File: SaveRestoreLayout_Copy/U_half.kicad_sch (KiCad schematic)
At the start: 2 parts

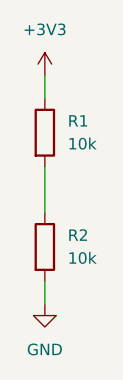
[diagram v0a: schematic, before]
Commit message: annotate the copy of SaveRestoreLayout_Copy/U_half.kicad_sch
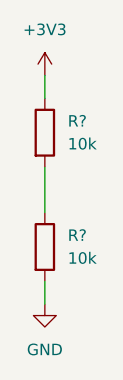
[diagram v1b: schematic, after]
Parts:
- renumbered R2 to R?, R1 to R?
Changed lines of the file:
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@@
   (symbol (lib_id "Device:R") (at 123.19 88.9 0) (unit 1)
     (in_bom yes) (on_board yes) (dnp no) (fields_autoplaced)
-    (property "Reference" "R2" (at 125.73 87.63 0)
+    (property "Reference" "R?" (at 125.73 87.63 0)
       (effects (font (size 1.27 1.27)) (justify left))
     )
@@
       (project "SaveRestoreLayout_Original"
         (path "/77dfa459-80c3-47cd-804e-1711acb5c83d/a587b1de-fcac-40bf-8a11-56b95432cd59"
-          (reference "R2") (unit 1)
+          (reference "R?") (unit 1)
+        )
+      )
+      (project "SaveRestoreLayout_Copy"
+        (path "/f7049a7e-2ee3-423f-8203-c90463fac327/9e96eef9-761d-4371-b289-d9fc0db18200"
+          (reference "R3") (unit 1)
         )
       )
@@
   (symbol (lib_id "power:+3V3") (at 123.19 69.85 0) (unit 1)
     (in_bom yes) (on_board yes) (dnp no) (fields_autoplaced)
-    (property "Reference" "#PWR03" (at 123.19 73.66 0)
+    (property "Reference" "#PWR?" (at 123.19 73.66 0)
       (effects (font (size 1.27 1.27)) hide)
     )
@@
       (project "SaveRestoreLayout_Original"
         (path "/77dfa459-80c3-47cd-804e-1711acb5c83d/a587b1de-fcac-40bf-8a11-56b95432cd59"
+          (reference "#PWR?") (unit 1)
+        )
+      )
+      (project "SaveRestoreLayout_Copy"
+        (path "/f7049a7e-2ee3-423f-8203-c90463fac327/9e96eef9-761d-4371-b289-d9fc0db18200"
           (reference "#PWR03") (unit 1)
         )
@@
   (symbol (lib_id "power:GND") (at 123.19 95.25 0) (unit 1)
     (in_bom yes) (on_board yes) (dnp no) (fields_autoplaced)
-    (property "Reference" "#PWR04" (at 123.19 101.6 0)
+    (property "Reference" "#PWR?" (at 123.19 101.6 0)
       (effects (font (size 1.27 1.27)) hide)
     )
@@
       (project "SaveRestoreLayout_Original"
         (path "/77dfa459-80c3-47cd-804e-1711acb5c83d/a587b1de-fcac-40bf-8a11-56b95432cd59"
+          (reference "#PWR?") (unit 1)
+        )
+      )
+      (project "SaveRestoreLayout_Copy"
+        (path "/f7049a7e-2ee3-423f-8203-c90463fac327/9e96eef9-761d-4371-b289-d9fc0db18200"
           (reference "#PWR04") (unit 1)
         )
@@
   (symbol (lib_id "Device:R") (at 123.19 76.2 0) (unit 1)
     (in_bom yes) (on_board yes) (dnp no) (fields_autoplaced)
-    (property "Reference" "R1" (at 125.73 74.93 0)
+    (property "Reference" "R?" (at 125.73 74.93 0)
       (effects (font (size 1.27 1.27)) (justify left))
     )
@@
       (project "SaveRestoreLayout_Original"
         (path "/77dfa459-80c3-47cd-804e-1711acb5c83d/a587b1de-fcac-40bf-8a11-56b95432cd59"
-          (reference "R1") (unit 1)
+          (reference "R?") (unit 1)
         )
       )
+      (project "SaveRestoreLayout_Copy"
+        (path "/f7049a7e-2ee3-423f-8203-c90463fac327/9e96eef9-761d-4371-b289-d9fc0db18200"
+          (reference "R2") (unit 1)
+        )
+      )

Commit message: restore the layour from original
bug: the bottom layout is not restored and no via is placed
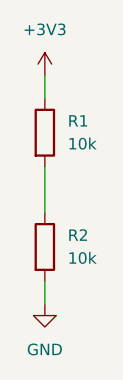
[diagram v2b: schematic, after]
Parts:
- gave numbers to parts that had none: 2
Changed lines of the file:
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@@
   (symbol (lib_id "Device:R") (at 123.19 88.9 0) (unit 1)
     (in_bom yes) (on_board yes) (dnp no) (fields_autoplaced)
-    (property "Reference" "R?" (at 125.73 87.63 0)
+    (property "Reference" "R2" (at 125.73 87.63 0)
       (effects (font (size 1.27 1.27)) (justify left))
     )
@@
       (project "SaveRestoreLayout_Original"
         (path "/77dfa459-80c3-47cd-804e-1711acb5c83d/a587b1de-fcac-40bf-8a11-56b95432cd59"
-          (reference "R?") (unit 1)
+          (reference "R2") (unit 1)
         )
       )
       (project "SaveRestoreLayout_Copy"
         (path "/f7049a7e-2ee3-423f-8203-c90463fac327/9e96eef9-761d-4371-b289-d9fc0db18200"
-          (reference "R3") (unit 1)
+          (reference "R2") (unit 1)
         )
       )
@@
   (symbol (lib_id "power:+3V3") (at 123.19 69.85 0) (unit 1)
     (in_bom yes) (on_board yes) (dnp no) (fields_autoplaced)
-    (property "Reference" "#PWR?" (at 123.19 73.66 0)
+    (property "Reference" "#PWR03" (at 123.19 73.66 0)
       (effects (font (size 1.27 1.27)) hide)
     )
@@
       (project "SaveRestoreLayout_Original"
         (path "/77dfa459-80c3-47cd-804e-1711acb5c83d/a587b1de-fcac-40bf-8a11-56b95432cd59"
-          (reference "#PWR?") (unit 1)
+          (reference "#PWR03") (unit 1)
         )
       )
@@
   (symbol (lib_id "power:GND") (at 123.19 95.25 0) (unit 1)
     (in_bom yes) (on_board yes) (dnp no) (fields_autoplaced)
-    (property "Reference" "#PWR?" (at 123.19 101.6 0)
+    (property "Reference" "#PWR04" (at 123.19 101.6 0)
       (effects (font (size 1.27 1.27)) hide)
     )
@@
       (project "SaveRestoreLayout_Original"
         (path "/77dfa459-80c3-47cd-804e-1711acb5c83d/a587b1de-fcac-40bf-8a11-56b95432cd59"
-          (reference "#PWR?") (unit 1)
+          (reference "#PWR04") (unit 1)
         )
       )
@@
   (symbol (lib_id "Device:R") (at 123.19 76.2 0) (unit 1)
     (in_bom yes) (on_board yes) (dnp no) (fields_autoplaced)
-    (property "Reference" "R?" (at 125.73 74.93 0)
+    (property "Reference" "R1" (at 125.73 74.93 0)
       (effects (font (size 1.27 1.27)) (justify left))
     )
@@
       (project "SaveRestoreLayout_Original"
         (path "/77dfa459-80c3-47cd-804e-1711acb5c83d/a587b1de-fcac-40bf-8a11-56b95432cd59"
-          (reference "R?") (unit 1)
+          (reference "R1") (unit 1)
         )
       )
       (project "SaveRestoreLayout_Copy"
         (path "/f7049a7e-2ee3-423f-8203-c90463fac327/9e96eef9-761d-4371-b289-d9fc0db18200"
-          (reference "R2") (unit 1)
+          (reference "R1") (unit 1)
         )
       )
